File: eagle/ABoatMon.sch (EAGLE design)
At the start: 17 parts, among them J1 5V, J2 GND, J3 GND

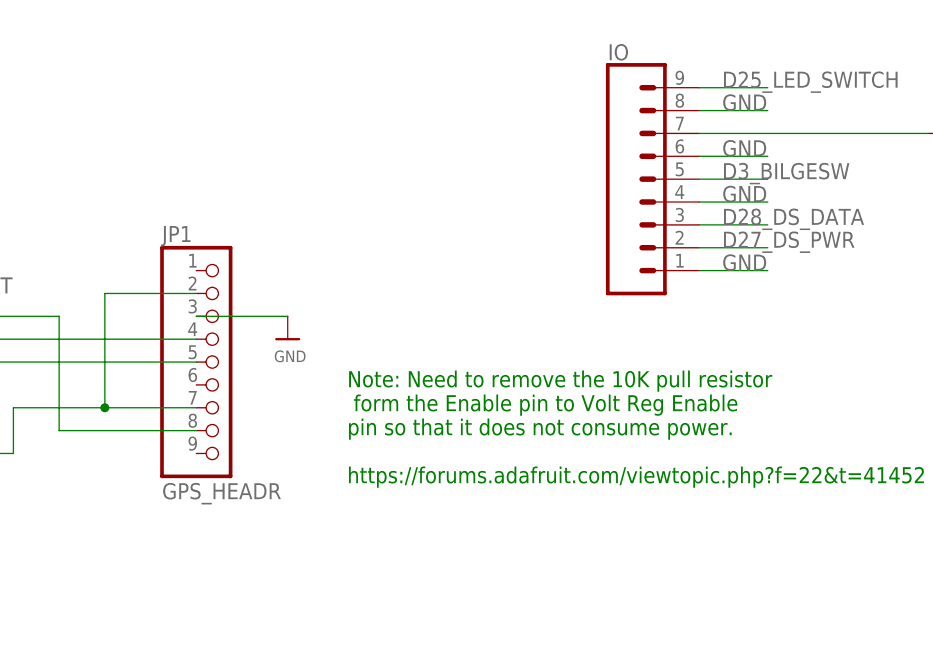
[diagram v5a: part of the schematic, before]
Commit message: Silkscreen updates
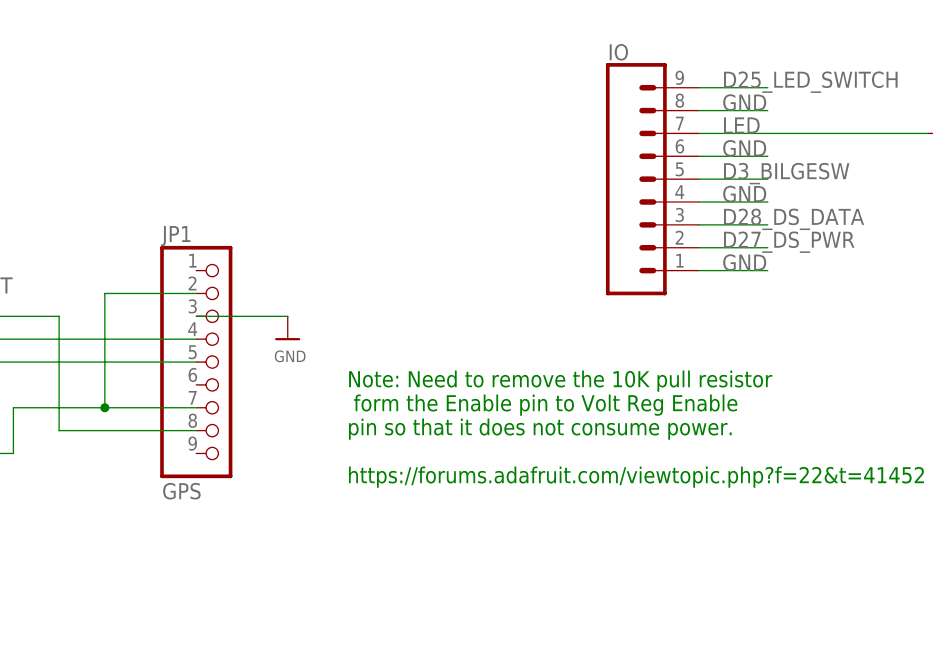
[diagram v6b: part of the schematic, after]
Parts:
- JP1: value GPS_HEADR -> GPS
- renumbered VCC to ENABLE
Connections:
- net N$2 renamed LED
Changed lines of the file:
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@@
 <parts>
 <part name="U$12" library="microbuilder" deviceset="GND" device=""/>
-<part name="JP1" library="microbuilder" deviceset="HEADER-1X9" device="70MIL" value="GPS_HEADR"/>
+<part name="JP1" library="microbuilder" deviceset="HEADER-1X9" device="70MIL" value="GPS"/>
 <part name="JST1" library="adafruit" deviceset="JST_2PIN" device="-THM" value="LIPO"/>
 <part name="SUPPLY2" library="supply2" deviceset="GND" device=""/>
@@
 <part name="C2" library="SparkFun-Capacitors" deviceset="0.1UF" device="-KIT-EZ-50V-20%" value="0.1U"/>
 <part name="R5" library="SparkFun-Resistors" deviceset="1KOHM" device="-HORIZ-1/4W-1%" value="3.3M"/>
-<part name="VCC" library="SparkFun-Connectors" deviceset="CONN_02" device="" value="VCC"/>
+<part name="ENABLE" library="SparkFun-Connectors" deviceset="CONN_02" device="" value="VCC"/>
 <part name="SUPPLY9" library="supply2" deviceset="GND" device=""/>
 <part name="JST_PWR" library="SparkFun-Connectors" deviceset="CONN_04" device="JST-PTH" value="VVC_5V"/>
@@
 <instance part="C2" gate="G$1" x="198.12" y="50.8"/>
 <instance part="R5" gate="G$1" x="187.96" y="50.8" rot="R90"/>
-<instance part="VCC" gate="G$1" x="223.52" y="71.12" smashed="yes" rot="R180">
+<instance part="ENABLE" gate="G$1" x="223.52" y="71.12" smashed="yes" rot="R180">
 <attribute name="VALUE" x="226.06" y="65.786" size="1.778" layer="96" font="vector" rot="R180"/>
 </instance>
@@
 </segment>
 <segment>
-<pinref part="VCC" gate="G$1" pin="1"/>
+<pinref part="ENABLE" gate="G$1" pin="1"/>
 <wire x1="215.9" y1="71.12" x2="208.28" y2="71.12" width="0.1524" layer="91"/>
 <label x="208.28" y="71.12" size="1.778" layer="95"/>
@@
 <wire x1="180.34" y1="68.58" x2="180.34" y2="48.26" width="0.1524" layer="91"/>
 <label x="180.34" y="55.88" size="1.778" layer="95" rot="R90"/>
-<pinref part="VCC" gate="G$1" pin="2"/>
+<pinref part="ENABLE" gate="G$1" pin="2"/>
 <pinref part="JST_PWR" gate="G$1" pin="4"/>
 <wire x1="180.34" y1="68.58" x2="187.96" y2="68.58" width="0.1524" layer="91"/>
@@
 </segment>
 </net>
-<net name="N$2" class="0">
+<net name="LED" class="0">
 <segment>
 <wire x1="205.74" y1="154.94" x2="231.14" y2="154.94" width="0.1524" layer="91"/>
 <pinref part="R7" gate="G$1" pin="1"/>
 <pinref part="IO" gate="G$1" pin="7"/>
-</segment>
-</net>
+<label x="208.28" y="154.94" size="1.778" layer="95"/>
+</segment>
+</net>

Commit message: v2.99 - complete relayout
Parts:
- removed IO: (no value), SparkFun-Connectors:CONN_09
- removed JST_PWR: VVC_5V, SparkFun-Connectors:CONN_04JST-PTH
- added LIPO, VCC: (no value), microbuilder:HEADER-1X2ROUND
- added U$2, U$3, U$4, U$5: MOUNTINGHOLE2.5, microbuilder:MOUNTINGHOLE2.5
- added X1, X2, X3: (no value), con-wago-500:W237-103
- added X4: (no value), con-wago-500:W237-4
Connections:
- new net VCC_JUMPER: ENABLE.2, VCC.1
- new net VIN_JUMPER: JST1.2, LIPO.2, R2.2
- net 5V: now also X4-3.KL; no longer JST_PWR.2
- net D25_LED_SWITCH: now also X1-1.KL; no longer IO.9
- net D27_DS_PWR: now also X3-2.KL; no longer IO.2
- net D28_DS_DATA: now also X3-1.KL; no longer IO.3
- net D3_BILGESW: now also X2-2.KL; no longer IO.5
- net GND: now also MOTEINO_MEGA.GND2, X1-2.KL, X2-1.KL, X2-3.KL, X3-3.KL, X4-2.KL, X4-4.KL; no longer IO.1, IO.4, IO.6, IO.8, JST_PWR.1, JST_PWR.3
- net LED: now also X1-3.KL; no longer IO.7
- net VCC: now also VCC.2, X4-1.KL; no longer ENABLE.2, JST_PWR.4
- net VIN: now also LIPO.1; no longer JST1.2, R2.2
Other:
- note added: "Mini Step Down Voltage Reg Holtek HT7463A 6v~55V VCC 5V Output Max 600mA, 96% eff"
- note added: "Note: Need to remove the 10K pull resistor from the Enable pin to Volt Reg Enable pin so that it does not consume power. https://forums.adafruit.com/viewtopic.php?f=22&t=41452"
- note removed: "Mini Step Down Voltage Reg Buck Module 4.5v~55V VCC 5V Output Max 600mA, 96% eff"
- note removed: "Note: Need to remove the 10K pull resistor form the Enable pin to Volt Reg Enable pin so that it does not consume power. https://forums.adafruit.com/viewtopic.php?f=22&t=41452"
- moved on the sheet: C1, J1, JST1, R2, R3, R6, R7

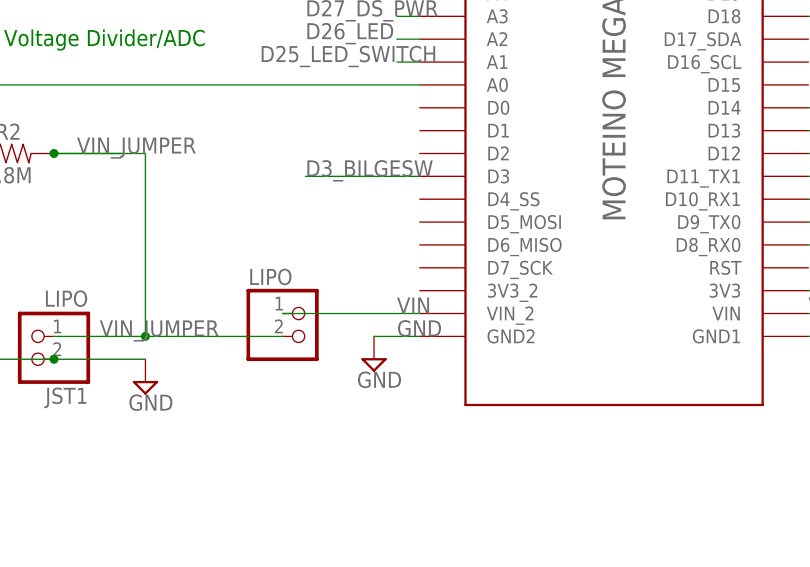
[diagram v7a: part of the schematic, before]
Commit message: Added the other 3v rail, silkscreen fixes
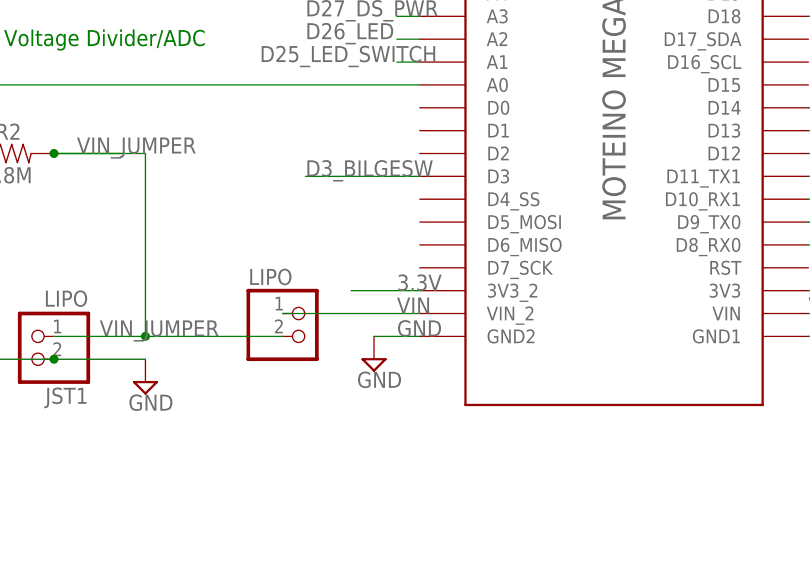
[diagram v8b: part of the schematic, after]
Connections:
- net 3.3V: now also MOTEINO_MEGA.3V3_2
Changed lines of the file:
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@@
 <attributes>
 <attribute name="CNAME" value="MoteinoMega ABoatMon Shield"/>
-<attribute name="CREVISION" value="2.99"/>
+<attribute name="CREVISION" value="0.399"/>
 <attribute name="DESIGNER" value="greg.cope@gmail.com"/>
 </attributes>
@@
 <junction x="139.7" y="124.46"/>
 </segment>
-</net>
+<segment>
+<pinref part="MOTEINO_MEGA" gate="G$1" pin="3V3_2"/>
+<wire x1="63.5" y1="119.38" x2="55.88" y2="119.38" width="0.1524" layer="91"/>
+<label x="60.96" y="119.38" size="1.778" layer="95"/>
+</segment>
+</net>
